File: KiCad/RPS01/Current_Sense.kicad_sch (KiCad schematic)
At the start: 4 parts, among them U12 INA139QPWRQ1

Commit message: Huge PCB Update
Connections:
- net Load: now also R1.2; no longer U12.2 (VIN+)
- net Vp: now reaches R1.1
- net Vp: now also U12.2 (VIN+)
- no-connect marks 5 -> 3
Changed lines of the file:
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@@
   (junction (at 111.76 101.6158) (diameter 0) (color 0 0 0 0)
   )
-  (no_connect (at 105.156 23.622))
   (no_connect (at 101.6 97.79))
-  (no_connect (at 112.776 23.622))
   (no_connect (at 104.14 41.91))
   (no_connect (at 106.68 97.79))
   (wire (pts (xy 121.92 101.6158) (xy 133.35 101.6158))
+    (stroke (width 0) (type default))
+  )
+  (wire (pts (xy 105.156 23.622) (xy 104.14 23.622))
+    (stroke (width 0) (type default))
+  )
+  (wire (pts (xy 114.046 23.622) (xy 114.046 35.56))
     (stroke (width 0) (type default))
   )
@@
     (stroke (width 0) (type default))
   )
-  (wire (pts (xy 114.046 25.654) (xy 114.046 35.56))
-    (stroke (width 0) (type default))
-  )
   (wire (pts (xy 101.6 41.91) (xy 81.28 41.91))
     (stroke (width 0) (type default))
@@
     (stroke (width 0) (type default))
   )
-  (wire (pts (xy 104.14 35.56) (xy 104.14 25.654))
+  (wire (pts (xy 104.14 23.622) (xy 104.14 35.56))
     (stroke (width 0) (type default))
   )
@@
   )
   (wire (pts (xy 111.76 101.6158) (xy 121.92 101.6158))
+    (stroke (width 0) (type default))
+  )
+  (wire (pts (xy 112.776 23.622) (xy 114.046 23.622))
     (stroke (width 0) (type default))
   )
@@
     (stroke (width 0) (type default))
   )
-  (wire (pts (xy 104.14 25.654) (xy 114.046 25.654))
-    (stroke (width 0) (type default))
-  )

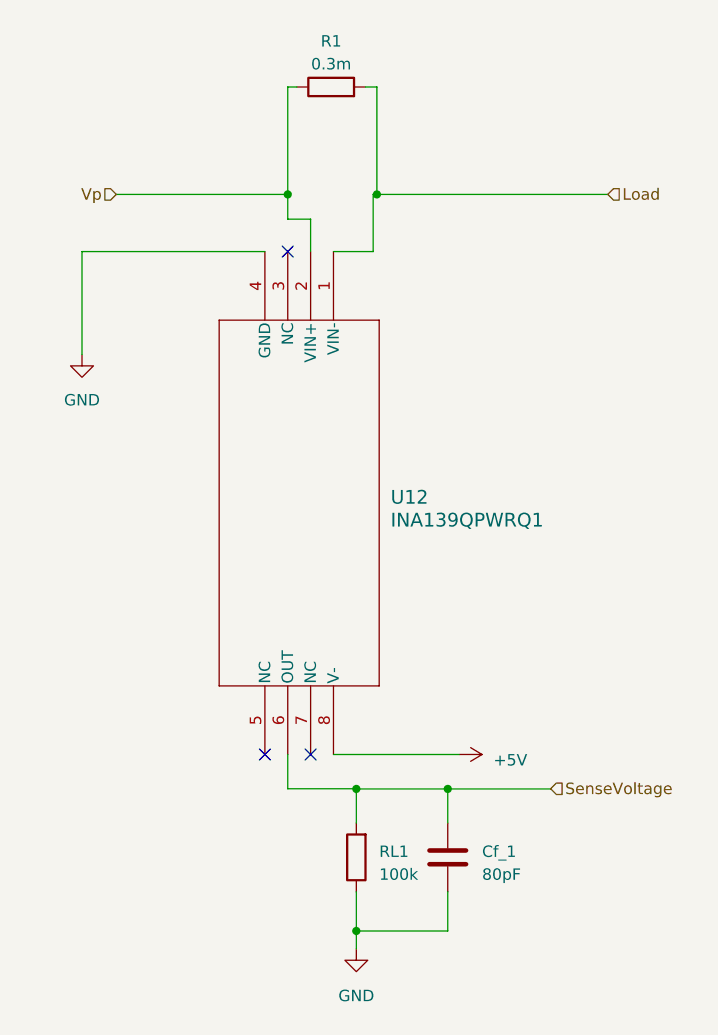
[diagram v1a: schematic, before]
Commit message: Finished Load Sharing and Current Sense
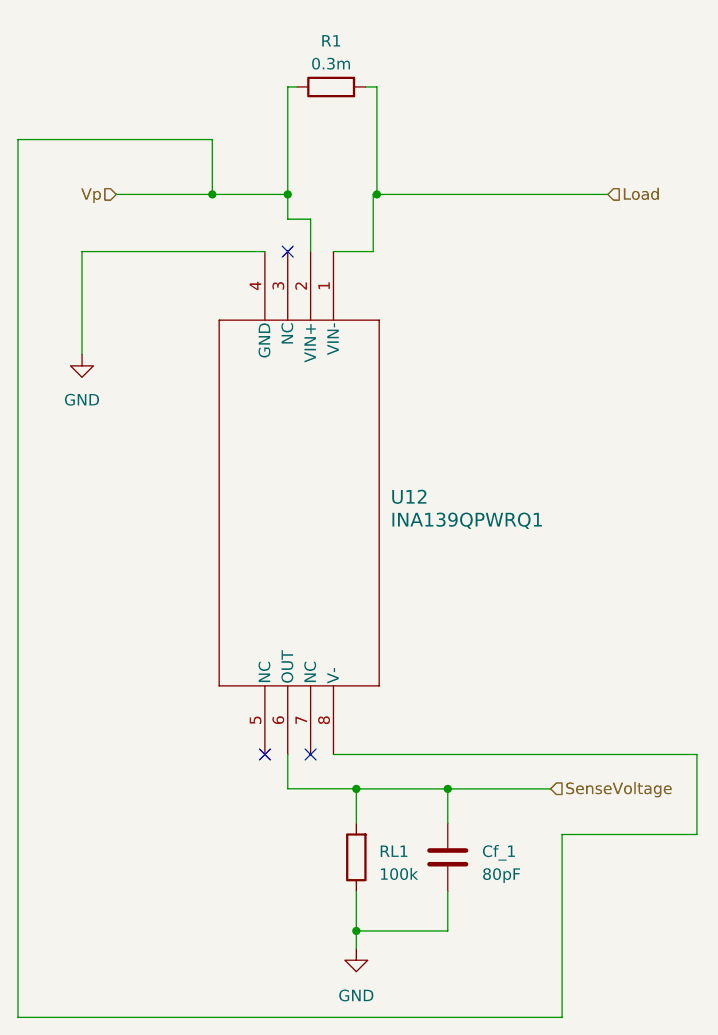
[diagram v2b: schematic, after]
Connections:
- net +5V is gone; now on net Vp: U12.8 (V-)
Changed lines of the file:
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@@
   (junction (at 111.76 117.3986) (diameter 0) (color 0 0 0 0)
   )
+  (junction (at 95.758 35.56) (diameter 0) (color 0 0 0 0)
+  )
   (junction (at 114.046 35.56) (diameter 0) (color 0 0 0 0)
   )
@@
     (stroke (width 0) (type default))
   )
+  (wire (pts (xy 74.168 127) (xy 74.168 29.464))
+    (stroke (width 0) (type default))
+  )
+  (wire (pts (xy 149.606 97.79) (xy 149.606 106.68))
+    (stroke (width 0) (type default))
+  )
   (wire (pts (xy 105.156 23.622) (xy 104.14 23.622))
     (stroke (width 0) (type default))
@@
     (stroke (width 0) (type default))
   )
-  (wire (pts (xy 85.09 35.56) (xy 104.14 35.56))
+  (wire (pts (xy 85.09 35.56) (xy 95.758 35.56))
     (stroke (width 0) (type default))
   )
@@
     (stroke (width 0) (type default))
   )
-  (wire (pts (xy 109.22 97.79) (xy 123.19 97.79))
+  (wire (pts (xy 109.22 97.79) (xy 149.606 97.79))
     (stroke (width 0) (type default))
   )
@@
     (stroke (width 0) (type default))
   )
+  (wire (pts (xy 134.62 127) (xy 74.168 127))
+    (stroke (width 0) (type default))
+  )
+  (wire (pts (xy 74.168 29.464) (xy 95.758 29.464))
+    (stroke (width 0) (type default))
+  )
   (wire (pts (xy 112.776 23.622) (xy 114.046 23.622))
     (stroke (width 0) (type default))
@@
     (stroke (width 0) (type default))
   )
+  (wire (pts (xy 95.758 29.464) (xy 95.758 35.56))
+    (stroke (width 0) (type default))
+  )
+  (wire (pts (xy 134.62 106.68) (xy 134.62 127))
+    (stroke (width 0) (type default))
+  )
+  (wire (pts (xy 149.606 106.68) (xy 134.62 106.68))
+    (stroke (width 0) (type default))
+  )
   (wire (pts (xy 133.35 101.6158) (xy 133.35 101.6))
     (stroke (width 0) (type default))
@@
     (stroke (width 0) (type default))
   )
+  (wire (pts (xy 95.758 35.56) (xy 104.14 35.56))
+    (stroke (width 0) (type default))
+  )
   (image (at 190.2968 139.2682) (scale 1.22369)
     (data
@@
         )
       )
-    )
-  )
-  (symbol (lib_id "power:+5V") (at 123.19 97.79 270) (unit 1)
-    (in_bom yes) (on_board yes) (dnp no) (fields_autoplaced)
-    (property "Reference" "#PWR031" (at 119.38 97.79 0)
-      (effects (font (size 1.27 1.27)) hide)
-    )
-    (property "Value" "+5V" (at 127 98.425 90)
-      (effects (font (size 1.27 1.27)) (justify left))
-    )
-    (property "Footprint" "" (at 123.19 97.79 0)
-      (effects (font (size 1.27 1.27)) hide)
-    )
-    (property "Datasheet" "" (at 123.19 97.79 0)
-      (effects (font (size 1.27 1.27)) hide)
-    )
-    (pin "1")
-    (instances
-      (project "rps01"
-        (path "/14930f15-c0a0-4b55-93e6-b112548415f6/13e150ee-6c46-47a5-9c09-3749eb0dcbfe"
-          (reference "#PWR031") (unit 1)
-        )
-      )

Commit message: Large Schematic Update
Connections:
- net Load renamed LOAD
- net SenseVoltage renamed VSIG
- net Vp renamed VIN
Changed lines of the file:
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@@
     )
   )
-  (hierarchical_label "Load" (shape input) (at 139.7 35.56 0) (fields_autoplaced)
+  (hierarchical_label "LOAD" (shape input) (at 139.7 35.56 0) (fields_autoplaced)
     (effects (font (size 1.27 1.27)) (justify left))
   )
-  (hierarchical_label "SenseVoltage" (shape input) (at 133.35 101.6 0) (fields_autoplaced)
+  (hierarchical_label "VSIG" (shape input) (at 133.35 101.6 0) (fields_autoplaced)
     (effects (font (size 1.27 1.27)) (justify left))
   )
-  (hierarchical_label "Vp" (shape input) (at 85.09 35.56 180) (fields_autoplaced)
+  (hierarchical_label "VIN" (shape input) (at 85.09 35.56 180) (fields_autoplaced)
     (effects (font (size 1.27 1.27)) (justify right))
   )

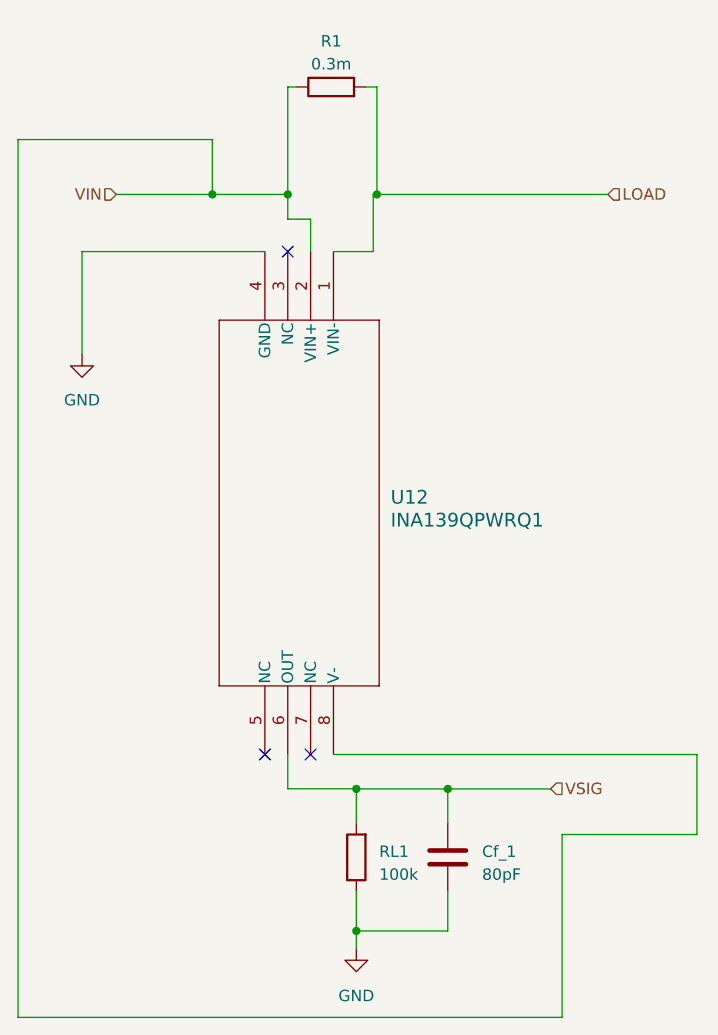
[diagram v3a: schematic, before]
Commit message: Finished most of the Schematics. Needs polishing
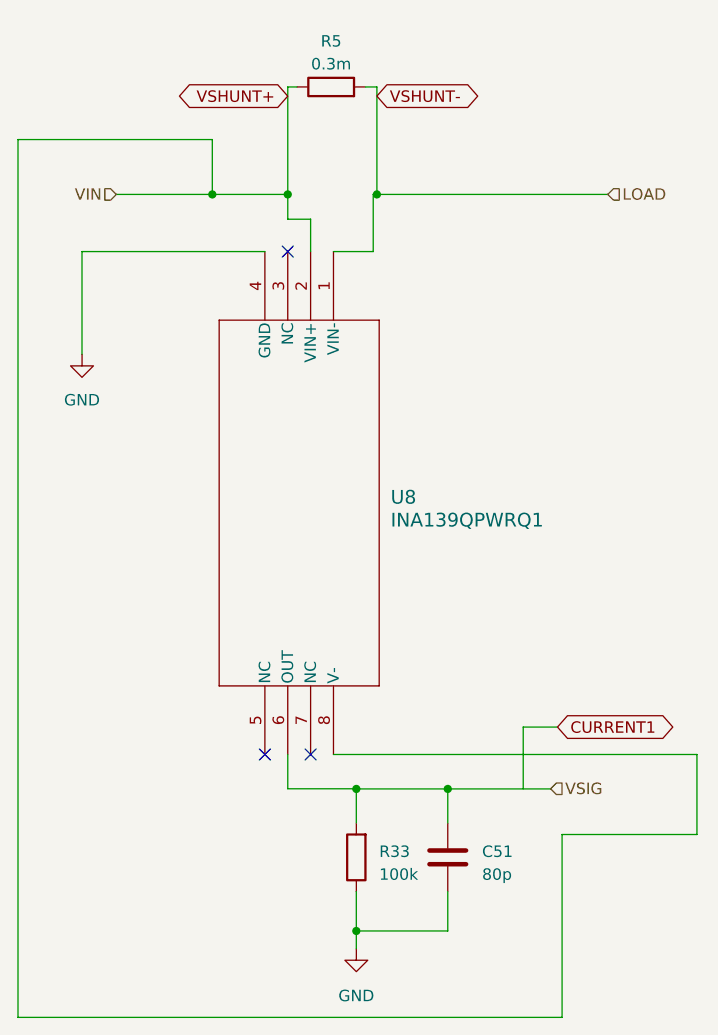
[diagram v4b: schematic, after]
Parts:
- C51: renamed from Cf_1; value 80pF -> 80p
- renumbered RL1 to R33, R1 to R5, U12 to U8
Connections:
- net LOAD renamed VSHUNT-
- net VIN renamed VSHUNT+
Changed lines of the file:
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@@
     (stroke (width 0) (type default))
   )
+  (wire (pts (xy 130.302 101.6) (xy 130.302 94.742))
+    (stroke (width 0) (type default))
+  )
   (wire (pts (xy 104.14 101.6) (xy 111.76 101.6))
     (stroke (width 0) (type default))
   )
+  (wire (pts (xy 130.302 94.742) (xy 134.112 94.742))
+    (stroke (width 0) (type default))
+  )
   (wire (pts (xy 121.92 101.6158) (xy 121.92 105.41))
     (stroke (width 0) (type default))
@@
     )
   )
+  (global_label "VSHUNT-" (shape bidirectional) (at 114.046 24.638 0) (fields_autoplaced)
+    (effects (font (size 1.27 1.27)) (justify left))
+    (property "Intersheetrefs" "${INTERSHEET_REFS}" (at 126.8927 24.638 0)
+      (effects (font (size 1.27 1.27)) (justify left) hide)
+    )
+  )
+  (global_label "VSHUNT+" (shape bidirectional) (at 104.14 24.638 180) (fields_autoplaced)
+    (effects (font (size 1.27 1.27)) (justify right))
+    (property "Intersheetrefs" "${INTERSHEET_REFS}" (at 91.2933 24.638 0)
+      (effects (font (size 1.27 1.27)) (justify right) hide)
+    )
+  )
+  (global_label "CURRENT1" (shape bidirectional) (at 134.112 94.742 0) (fields_autoplaced)
+    (effects (font (size 1.27 1.27)) (justify left))
+    (property "Intersheetrefs" "${INTERSHEET_REFS}" (at 147.9262 94.742 0)
+      (effects (font (size 1.27 1.27)) (justify left) hide)
+    )
+  )
   (hierarchical_label "LOAD" (shape input) (at 139.7 35.56 0) (fields_autoplaced)
     (effects (font (size 1.27 1.27)) (justify left))
@@
   (symbol (lib_id "power:GND") (at 81.28 53.34 0) (unit 1)
     (in_bom yes) (on_board yes) (dnp no) (fields_autoplaced)
-    (property "Reference" "#PWR030" (at 81.28 59.69 0)
+    (property "Reference" "#PWR012" (at 81.28 59.69 0)
       (effects (font (size 1.27 1.27)) hide)
     )
@@
       (project "rps01"
         (path "/14930f15-c0a0-4b55-93e6-b112548415f6/13e150ee-6c46-47a5-9c09-3749eb0dcbfe"
-          (reference "#PWR030") (unit 1)
+          (reference "#PWR012") (unit 1)
         )
       )
@@
   (symbol (lib_id "Device:R") (at 108.966 23.622 90) (unit 1)
     (in_bom yes) (on_board yes) (dnp no) (fields_autoplaced)
-    (property "Reference" "R1" (at 108.966 18.542 90)
+    (property "Reference" "R5" (at 108.966 18.542 90)
       (effects (font (size 1.27 1.27)))
     )
@@
       (project "rps01"
         (path "/14930f15-c0a0-4b55-93e6-b112548415f6/13e150ee-6c46-47a5-9c09-3749eb0dcbfe"
-          (reference "R1") (unit 1)
+          (reference "R5") (unit 1)
         )
       )
@@
   (symbol (lib_id "Device:C") (at 121.92 109.22 0) (unit 1)
     (in_bom yes) (on_board yes) (dnp no) (fields_autoplaced)
-    (property "Reference" "Cf_1" (at 125.73 108.585 0)
+    (property "Reference" "C51" (at 125.73 108.585 0)
       (effects (font (size 1.27 1.27)) (justify left))
     )
-    (property "Value" "80pF" (at 125.73 111.125 0)
+    (property "Value" "80p" (at 125.73 111.125 0)
       (effects (font (size 1.27 1.27)) (justify left))
     )
@@
       (project "rps01"
         (path "/14930f15-c0a0-4b55-93e6-b112548415f6/13e150ee-6c46-47a5-9c09-3749eb0dcbfe"
-          (reference "Cf_1") (unit 1)
+          (reference "C51") (unit 1)
         )
       )
@@
   (symbol (lib_id "power:GND") (at 111.76 119.38 0) (unit 1)
     (in_bom yes) (on_board yes) (dnp no) (fields_autoplaced)
-    (property "Reference" "#PWR040" (at 111.76 125.73 0)
+    (property "Reference" "#PWR013" (at 111.76 125.73 0)
       (effects (font (size 1.27 1.27)) hide)
     )
@@
       (project "rps01"
         (path "/14930f15-c0a0-4b55-93e6-b112548415f6/13e150ee-6c46-47a5-9c09-3749eb0dcbfe"
-          (reference "#PWR040") (unit 1)
+          (reference "#PWR013") (unit 1)
         )
       )
@@
   (symbol (lib_id "INA139:INA139QPWRQ1") (at 109.22 41.91 270) (unit 1)
     (in_bom yes) (on_board yes) (dnp no) (fields_autoplaced)
-    (property "Reference" "U12" (at 115.57 69.215 90)
+    (property "Reference" "U8" (at 115.57 69.215 90)
       (effects (font (size 1.524 1.524)) (justify left))
     )
@@
       (project "rps01"
         (path "/14930f15-c0a0-4b55-93e6-b112548415f6/13e150ee-6c46-47a5-9c09-3749eb0dcbfe"
-          (reference "U12") (unit 1)
+          (reference "U8") (unit 1)
         )
       )
@@
   (symbol (lib_id "Device:R") (at 111.76 109.22 180) (unit 1)
     (in_bom yes) (on_board yes) (dnp no) (fields_autoplaced)
-    (property "Reference" "RL1" (at 114.3 108.585 0)
+    (property "Reference" "R33" (at 114.3 108.585 0)
       (effects (font (size 1.27 1.27)) (justify right))
     )
@@
       (project "rps01"
         (path "/14930f15-c0a0-4b55-93e6-b112548415f6/13e150ee-6c46-47a5-9c09-3749eb0dcbfe"
-          (reference "RL1") (unit 1)
+          (reference "R33") (unit 1)
         )
       )
